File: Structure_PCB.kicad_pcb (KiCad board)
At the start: 2 copper layers, 180 x 100 mm, 22 parts, among them J10 JST-GH 4Pin, J11 JST-GH 4Pin, J12 JST-GH 4Pin, J6 6620XX236022_662004236022, J9 Conn_02x04_Top_Bottom, K2 FINDER-30.22

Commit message: finished structure pcb
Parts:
- D6: moved to B.Cu
- K2: moved to F.Cu
- moved K2 77.6 mm to (191.1, 140.0)
- moved J6 72.5 mm to (220.7, 62.5)
- moved D6 70.2 mm to (191.1, 136.0), turned to 90 degrees
- moved J9 61.6 mm to (220.7, 134.9)
- moved H5 10.2 mm to (205.0, 75.0)
- moved H6 10.2 mm to (205.0, 125.0)
- moved D5 8.08 mm to (60.0, 88.8), turned to 90 degrees
- moved D4 7.85 mm to (60.0, 129.0), turned to -90 degrees
- moved F1 6.05 mm to (61.5, 100.0)
- moved H7 5.67 mm to (110.0, 125.0)
- moved H8 5.67 mm to (110.0, 75.0)
- moved H1 2.00 mm to (67.0, 136.0)
- moved H2 2.00 mm to (67.0, 64.0)
- moved H3 2.00 mm to (180.2, 136.0)
- moved H4 2.00 mm to (180.2, 64.0)
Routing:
- net /HCout: track 43.0 -> 0.00 mm
- net /HCin: track 32.6 -> 0.00 mm
- net /pre_fuse: track 55.3 -> 38.2 mm
- net /post_arm: track 93.3 -> 101.4 mm
- net GND: track 12.5 -> 7.53 mm, vias 7 -> 4
- net /PBin: track 5.95 -> 8.26 mm
- net /SBout: track 216.8 -> 218.9 mm
- net /SBin: track 5.95 -> 7.47 mm
- added copper zone on F.Cu, net /HCin
- added copper zone on B.Cu, net /HCout
- removed copper zone on F.Cu, net /post_arm
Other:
- outline, holes or cut-outs redrawn
- board text added: "JLCJLCJLCJLC"
- board text added: "RAPID Structure PCB v2"
- board text added: "c.d."
- board text added: "c.i.p."
- board text added: "charge leds"
- board text added: "pw. good"
- board text added: "s 0 s 1 s 2"
- board text removed: "charge in progress"
- board text removed: "charge ind leds"
- board text removed: "charging done"
- board text removed: "power good"
- board text removed: "stat 0 stat 1 stat 2"
- board text removed: "todo: thicker traces"

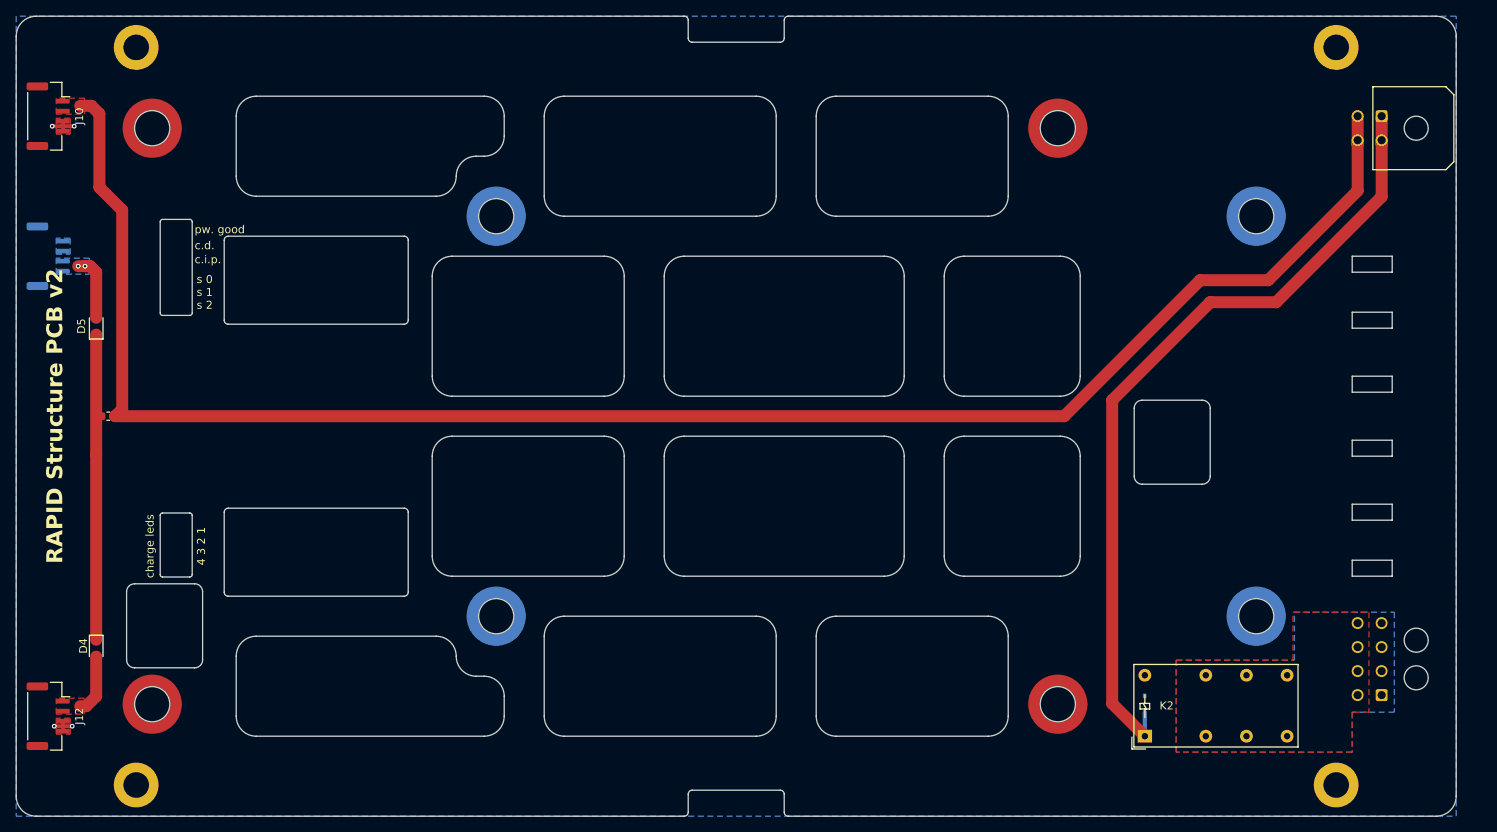
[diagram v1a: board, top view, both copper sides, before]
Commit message: added cats vega mounting
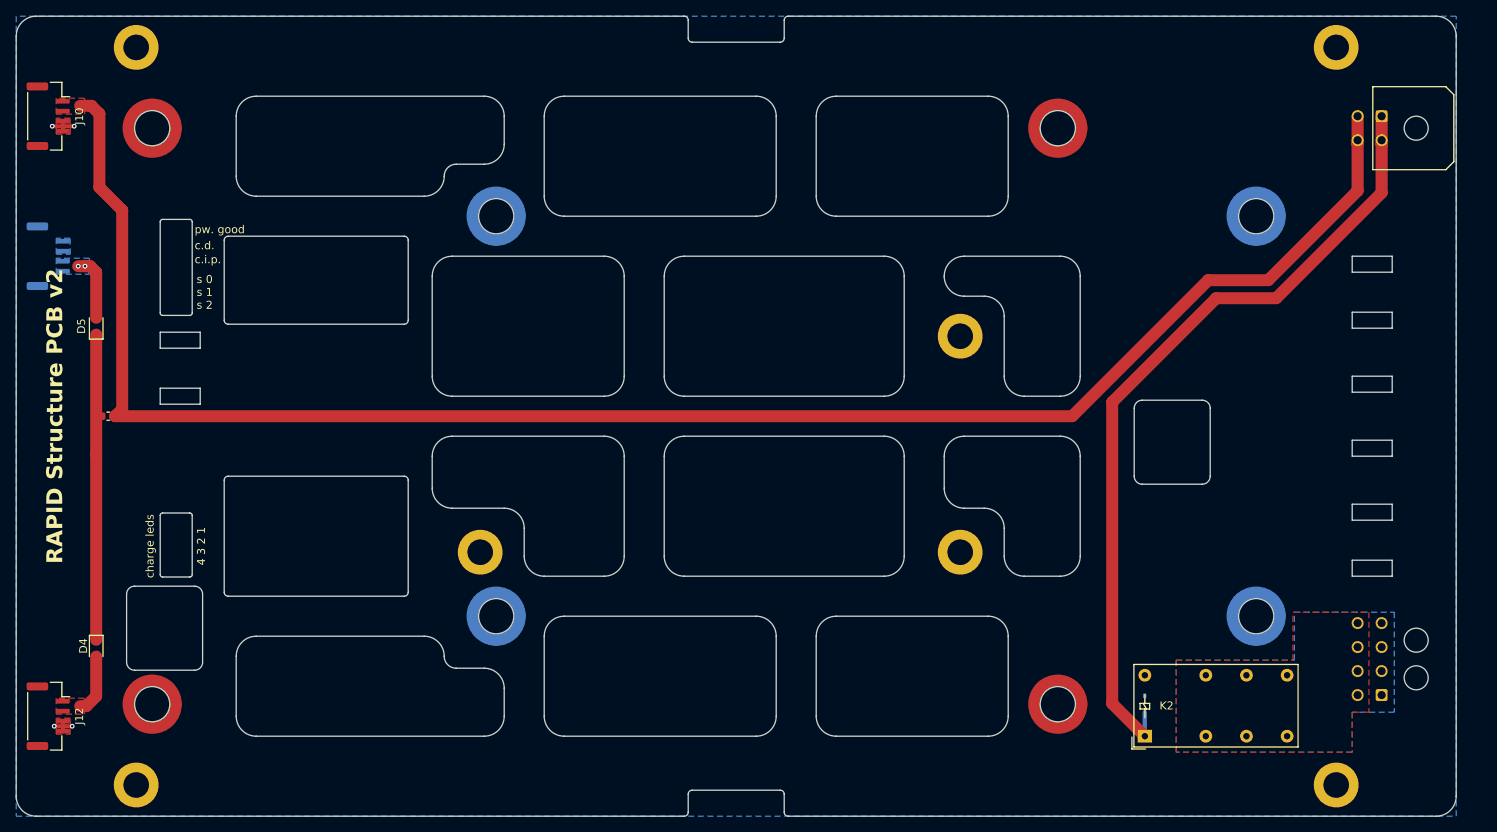
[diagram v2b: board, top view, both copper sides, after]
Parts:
- added H13: MountingHole, MountingHole:MountingHole_3.2mm_M3_DIN965_Pad, F.Cu at (108.0, 117.0)
- added H14: MountingHole, MountingHole:MountingHole_3.2mm_M3_DIN965_Pad, F.Cu at (168.0, 90.0)
- added H15: MountingHole, MountingHole:MountingHole_3.2mm_M3_DIN965_Pad, F.Cu at (168.0, 117.0)
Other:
- outline, holes or cut-outs redrawn
